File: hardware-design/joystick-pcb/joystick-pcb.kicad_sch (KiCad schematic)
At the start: 6 parts, among them J1 Wire_Pads, SW1 SKRHABE010

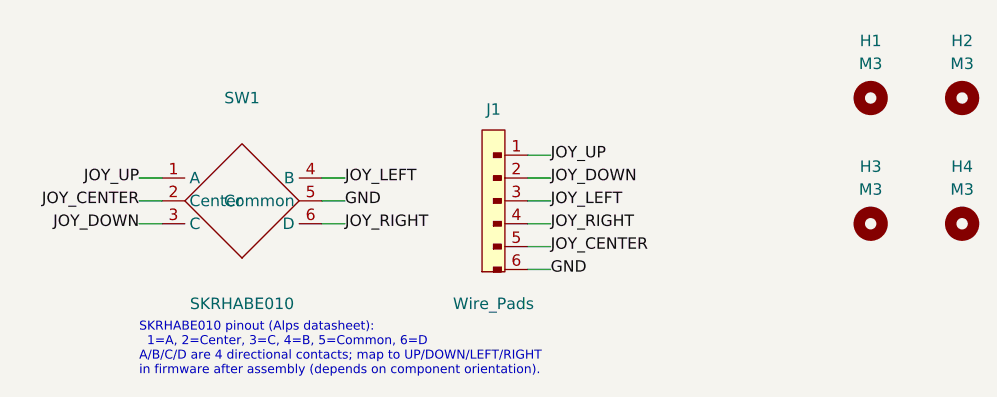
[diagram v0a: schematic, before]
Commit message: slight adjustments to pcb board for legibility
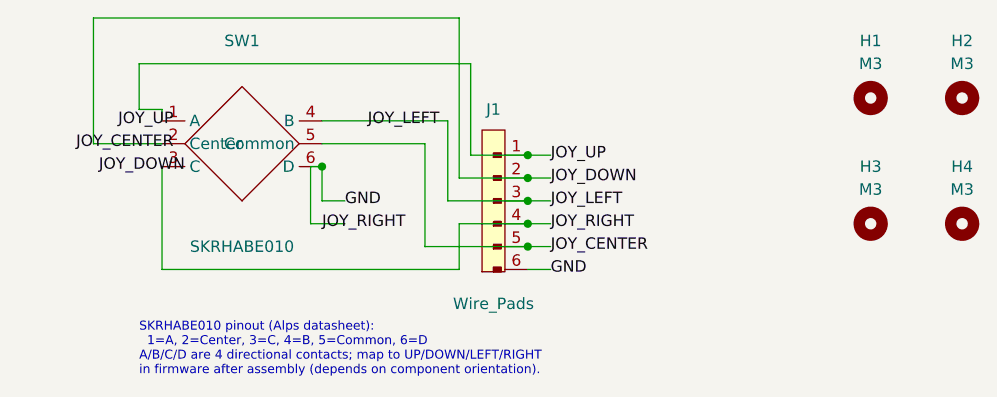
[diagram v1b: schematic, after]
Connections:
- net JOY_RIGHT is gone; now on net GND: J1.4 (Pin_4), SW1.6 (D)
- net GND: now also SW1.3 (C); no longer SW1.5 (Common)
- net JOY_CENTER: now also SW1.5 (Common); no longer SW1.2 (Center)
- net JOY_DOWN: now also SW1.2 (Center); no longer SW1.3 (C)
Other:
- moved on the sheet: SW1
